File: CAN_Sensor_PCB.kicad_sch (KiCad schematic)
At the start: 63 parts, among them J1 Conn_01x02, J3 Conn_01x02, J4 Conn_01x04, J5 Conn_01x04, U1 APM32F405RGT6, U2 LM2594HVM-3.3, U5 LMV358

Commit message: VER1.0: добавил BOM и закупочный лист
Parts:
- C19: Product Name (none) -> 293D107X96R3B2TE3
- D4: Description P/N Yellow LED -> LED
- D5: value MBRA320 -> ~; Description P/N (none) -> Diode; Product Name (none) -> MBRA320
- D6: Description P/N Blue LED -> LED
- D7: Description P/N Blue LED -> LED; Product Name FYLS-0805UBC -> FYLS-0805PGC
- J1: value Conn_01x02 -> ~; Purpose (none) -> CAN; now not fitted
- J3: value Conn_01x02 -> ~; Purpose (none) -> PWR; now not fitted
- J4: value Conn_01x04 -> ~; Purpose (none) -> PT1; now not fitted
- J5: value Conn_01x04 -> ~; Purpose (none) -> PT2; now not fitted
- L1: Product Name (none) -> NLC453232T-470K-PF
- U1: value APM32F405RGT6 -> ~; Product Name (none) -> APM32F405RGT6
- U2: value LM2594HVM-3.3 -> ~; Product Name (none) -> LM2594HVM-3.3
- U5: value LMV358 -> ~; Product Name (none) -> LM158DR
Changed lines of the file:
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@@
 			)
 		)
-		(property "Value" "LMV358"
+		(property "Value" "~"
 			(at 149.86 267.462 0)
 			(effects
@@
 			)
 		)
+		(property "Product Name" "LM158DR"
+			(at 148.844 261.62 0)
+			(effects
+				(font
+					(size 1.27 1.27)
+				)
+			)
+		)
 		(pin "2"
 		)
@@
 		(in_bom yes)
 		(on_board yes)
-		(dnp no)
+		(dnp yes)
 		(property "Reference" "J5"
 			(at 107.95 255.27 0)
@@
 			)
 		)
-		(property "Value" "Conn_01x04"
+		(property "Value" "~"
 			(at 107.95 254 0)
 			(effects
@@
 			)
 		)
+		(property "Purpose" "PT2"
+			(at 107.95 267.97 0)
+			(effects
+				(font
+					(size 1.27 1.27)
+				)
+			)
+		)
 		(pin "4"
 		)
@@
 			)
 		)
-		(property "Description P/N" "Blue LED"
+		(property "Description P/N" "LED"
 			(at 139.7 156.21 0)
 			(effects
@@
 			)
 		)
+		(property "Product Name" "293D107X96R3B2TE3"
+			(at 334.01 142.875 0)
+			(effects
+				(font
+					(size 1.27 1.27)
+				)
+				(hide yes)
+			)
+		)
 		(pin "1"
 		)
@@
 		(on_board yes)
 		(dnp no)
-		(fields_autoplaced yes)
 		(property "Reference" "U5"
 			(at 90.17 234.95 90)
@@
 			)
 		)
-		(property "Value" "LMV358"
+		(property "Value" "~"
 			(at 90.17 237.49 90)
 			(effects
@@
 			)
 		)
+		(property "Product Name" "LM158DR"
+			(at 90.17 237.49 90)
+			(effects
+				(font
+					(size 1.27 1.27)
+				)
+			)
+		)
 		(pin "2"
 		)
@@
 			)
 		)
-		(property "Description P/N" "Yellow LED"
+		(property "Description P/N" "LED"
 			(at 355.6 140.97 0)
 			(effects
@@
 			)
 		)
-		(property "Value" "LMV358"
+		(property "Value" "~"
 			(at 64.77 266.7 0)
 			(effects
@@
 			)
 		)
+		(property "Product Name" "LM158DR"
+			(at 63.5 261.62 0)
+			(effects
+				(font
+					(size 1.27 1.27)
+				)
+			)
+		)
 		(pin "2"
 		)
@@
 			)
 		)
-		(property "Value" "APM32F405RGT6"
+		(property "Value" "~"
 			(at 118.11 165.608 0)
 			(effects
@@
 			)
 		)
+		(property "Product Name" "APM32F405RGT6"
+			(at 113.03 118.11 0)
+			(effects
+				(font
+					(size 1.27 1.27)
+				)
+			)
+		)
 		(pin "60"
 		)
@@
 			)
 		)
-		(property "Value" "MBRA320"
+		(property "Value" "~"
 			(at 327.66 143.891 90)
 			(effects
@@
 			)
 		)
+		(property "Product Name" "MBRA320"
+			(at 325.12 142.24 0)
+			(effects
+				(font
+					(size 1.27 1.27)
+				)
+				(hide yes)
+			)
+		)
+		(property "Description P/N" "Diode"
+			(at 325.12 142.24 0)
+			(effects
+				(font
+					(size 1.27 1.27)
+				)
+				(hide yes)
+			)
+		)
 		(pin "1"
 		)
@@
 			)
 		)
+		(property "Product Name" "NLC453232T-470K-PF"
+			(at 328.93 138.43 0)
+			(effects
+				(font
+					(size 1.27 1.27)
+				)
+				(hide yes)
+			)
+		)
 		(pin "1"
 		)
@@
 		(in_bom yes)
 		(on_board yes)
-		(dnp no)
+		(dnp yes)
 		(property "Reference" "J1"
 			(at 340.36 67.31 0)
@@
 			)
 		)
-		(property "Value" "Conn_01x02"
+		(property "Value" "~"
 			(at 342.9 62.23 0)
 			(effects
@@
 			)
 		)
+		(property "Purpose" "CAN"
+			(at 342.9 71.12 0)
+			(effects
+				(font
+					(size 1.27 1.27)
+				)
+			)
+		)
 		(pin "2"
 		)
@@
 		(in_bom yes)
 		(on_board yes)
-		(dnp no)
+		(dnp yes)
 		(property "Reference" "J3"
 			(at 269.24 142.24 0)
@@
 			)
 		)
-		(property "Value" "Conn_01x02"
+		(property "Value" "~"
 			(at 271.78 137.16 0)
 			(effects
@@
 			)
 		)
+		(property "Purpose" "PWR"
+			(at 271.78 146.05 0)
+			(effects
+				(font
+					(size 1.27 1.27)
+				)
+			)
+		)
 		(pin "2"
 		)
@@
 			)
 		)
-		(property "Description P/N" "Blue LED"
+		(property "Description P/N" "LED"
 			(at 146.05 156.21 0)
 			(effects
@@
 			)
 		)
-		(property "Product Name" "FYLS-0805UBC"
+		(property "Product Name" "FYLS-0805PGC"
 			(at 146.05 156.21 0)
 			(effects
@@
 		(on_board yes)
 		(dnp no)
-		(fields_autoplaced yes)
 		(property "Reference" "U2"
 			(at 311.15 128.27 0)
@@
 			)
 		)
-		(property "Value" "LM2594HVM-3.3"
+		(property "Value" "~"
 			(at 311.15 130.81 0)
 			(effects
@@
 			)
 		)
+		(property "Product Name" "LM2594HVM-3.3"
+			(at 311.15 131.826 0)
+			(effects
+				(font
+					(size 1.27 1.27)
+				)
+			)
+		)
 		(pin "1"
 		)
@@
 		(in_bom yes)
 		(on_board yes)
-		(dnp no)
+		(dnp yes)
 		(property "Reference" "J4"
 			(at 22.86 255.27 0)
@@
 			)
 		)
-		(property "Value" "Conn_01x04"
+		(property "Value" "~"
 			(at 22.86 254 0)
 			(effects
@@
 			)
 		)
+		(property "Purpose" "PT1"
+			(at 22.86 267.97 0)
+			(effects
+				(font
+					(size 1.27 1.27)
+				)
+			)
+		)

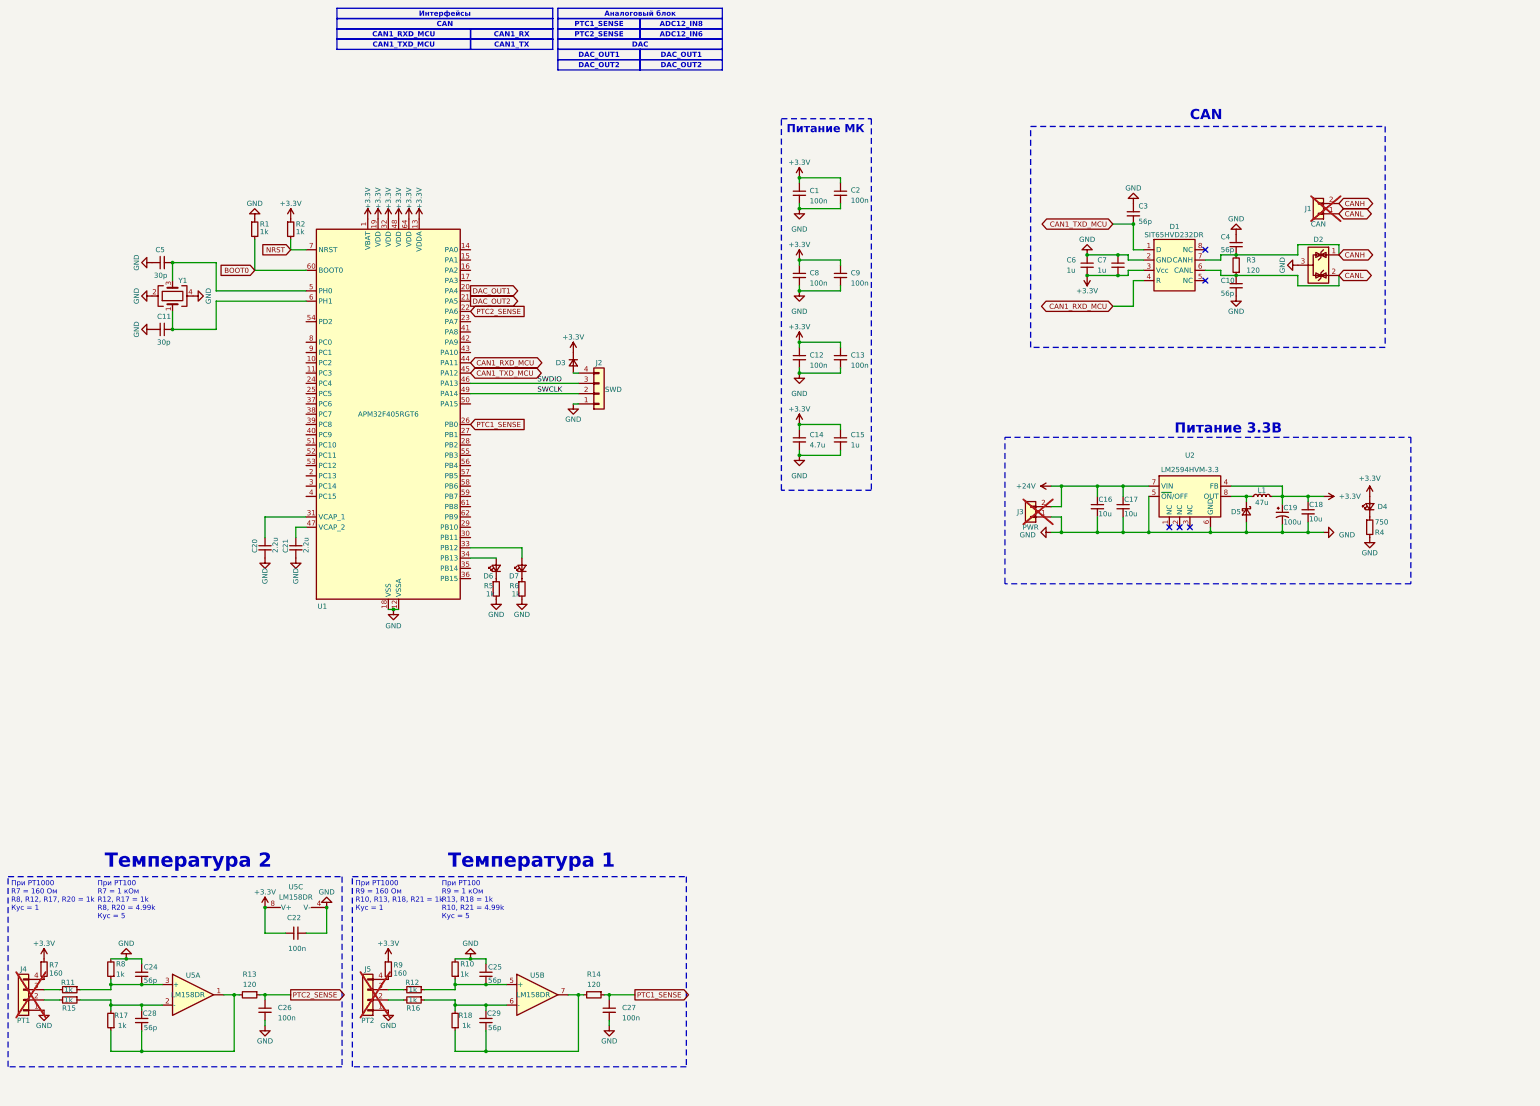
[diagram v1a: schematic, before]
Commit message: VER1.0: добавил схему по госту в доки
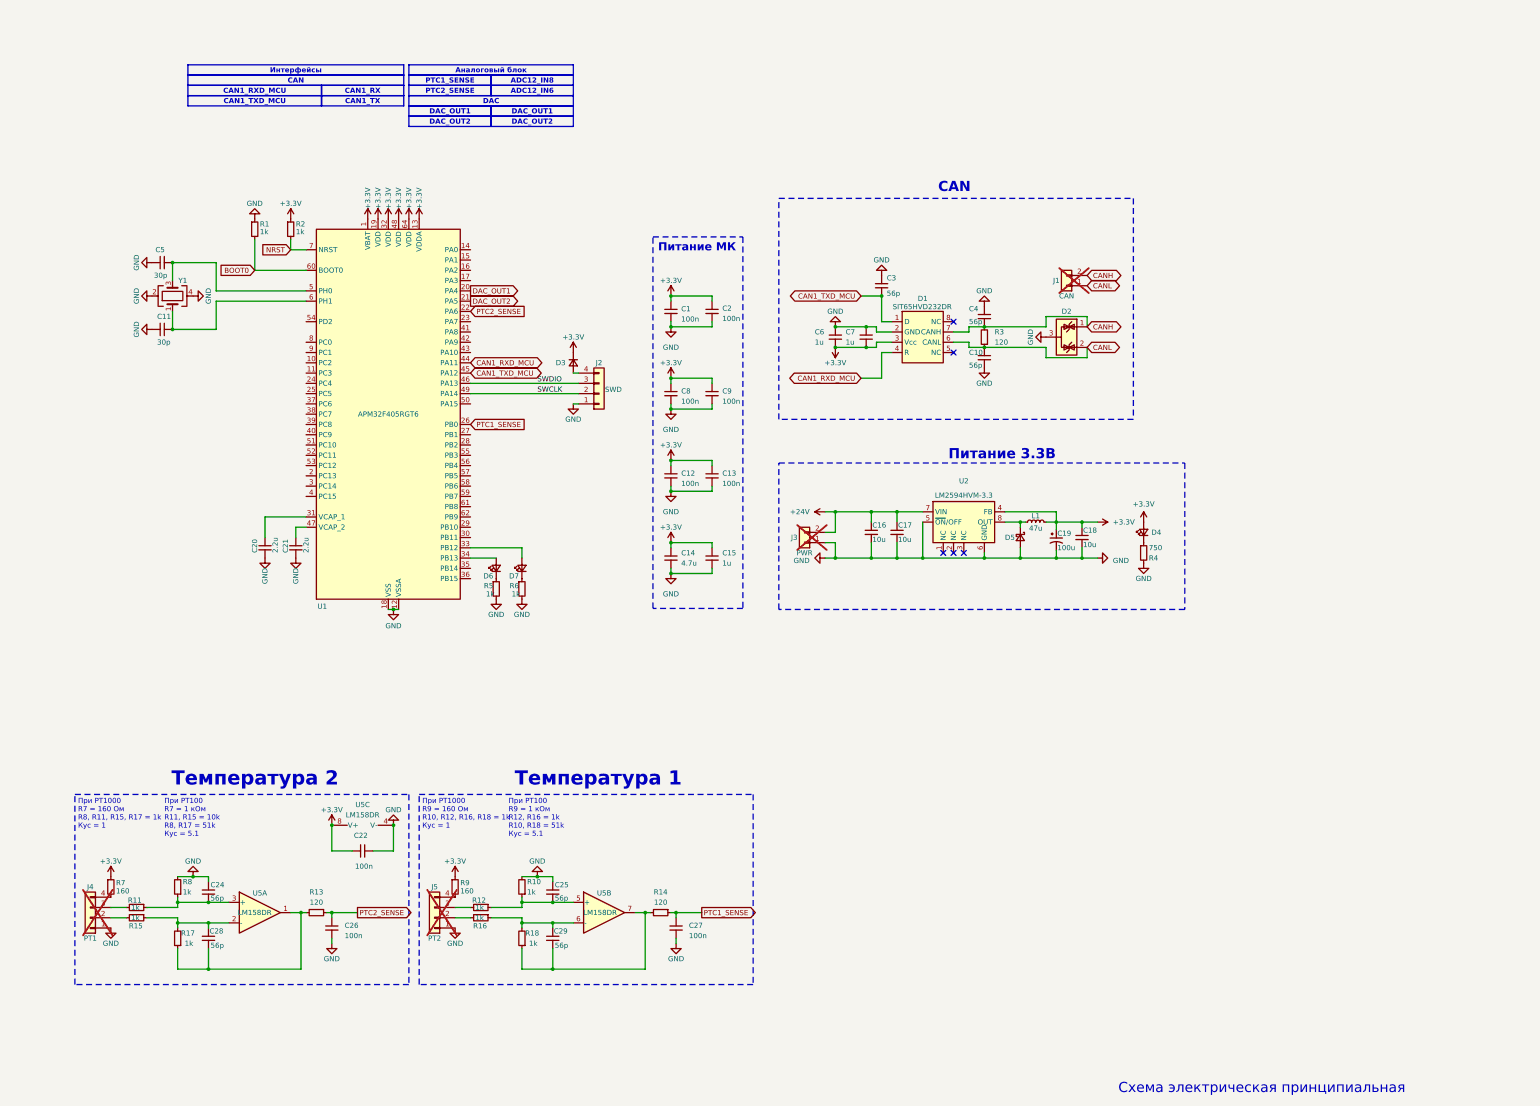
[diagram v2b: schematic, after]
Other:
- note added: "R10, R12, R16, R18 = 1k"
- note added: "R10, R18 = 51k"
- note added: "R11, R15 = 10k"
- note added: "R12, R16 = 1k"
- note added: "R8, R11, R15, R17 = 1k"
- note added: "R8, R17 = 51k"
- note added: "Кус = 5.1"
- note added: "Схема электрическая принципиальная"
- note removed: "R10, R13, R18, R21 = 1k"
- note removed: "R10, R21 = 4.99k"
- note removed: "R12, R17 = 1k"
- note removed: "R13, R18 = 1k"
- note removed: "R8, R12, R17, R20 = 1k"
- note removed: "R8, R20 = 4.99k"
- note removed: "Кус = 5"
- company: (none) -> ООО "Электротранспортные технологии"
- title: (none) -> Датчик температуры CAN
- moved on the sheet: C1, C10, C12, C13, C14, C15, C16, C17, C18, C19, C2, C22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

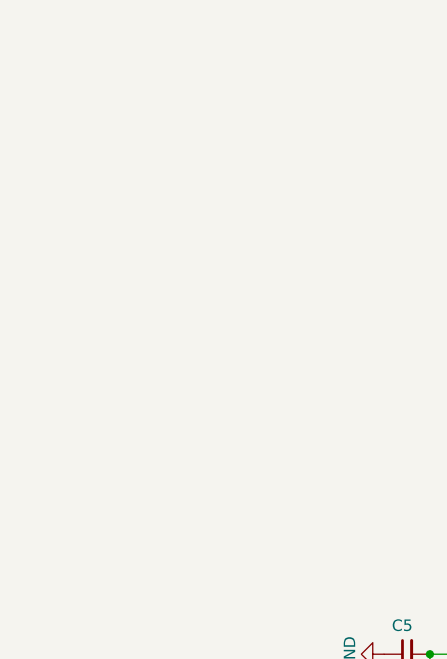
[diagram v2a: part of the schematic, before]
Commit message: VER1.0: исправил Э3
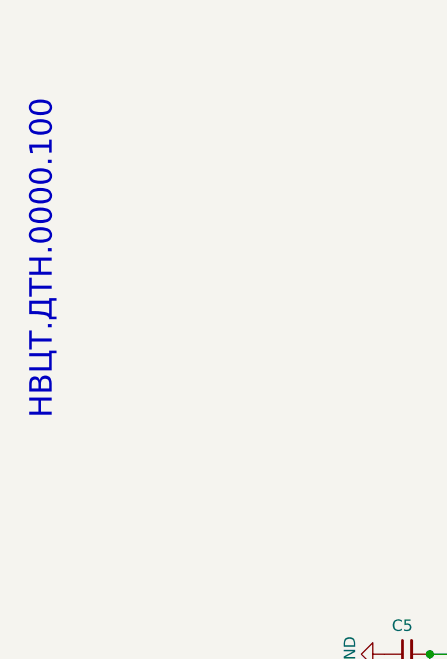
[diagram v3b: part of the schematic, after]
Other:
- note added: "НВЦТ.ДТН.0000.100"
- title: Датчик температуры CAN -> Плата датчика температуры CAN
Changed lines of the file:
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@@
 	(paper "A3")
 	(title_block
-		(title "Датчик температуры CAN")
+		(title "Плата датчика температуры CAN")
 		(company "ООО \"Электротранспортные технологии\"")
-		(comment 1 "НВЦТ.0001.0200.820 Э3")
+		(comment 1 "НВЦТ.ДТН.0000.100 Э3")
 		(comment 2 "Филатов А.С.")
 		(comment 3 "Сизякин А.В.")
@@
 		)
 	)
+	(text "НВЦТ.ДТН.0000.100"
+		(exclude_from_sim no)
+		(at 16.51 36.83 90)
+		(effects
+			(font
+				(size 2.5 2.5)
+			)
+		)
+	)

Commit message: VER21.0: исправил Э3
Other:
- note added: "1. Перечень элементов см. НВЦТ.ДТН.0000.100 ПЭ3."
- note added: "ООО "Электротранспортные"
- note added: "технологии""
- company: ООО "Электротранспортные технологии" -> (none)
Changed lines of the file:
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@@
 	(title_block
 		(title "Плата датчика температуры CAN")
-		(company "ООО \"Электротранспортные технологии\"")
 		(comment 1 "НВЦТ.ДТН.0000.100 Э3")
 		(comment 2 "Филатов А.С.")
@@
 	(text "Схема электрическая принципиальная"
 		(exclude_from_sim no)
-		(at 328.93 284.734 0)
+		(at 329.946 271.272 0)
 		(effects
 			(font
@@
 		)
 	)
+	(text "ООО \"Электротранспортные"
+		(exclude_from_sim no)
+		(at 389.89 282.702 0)
+		(effects
+			(font
+				(size 2.5 2.5)
+			)
+		)
+	)
 	(text "R9 = 160 Ом\n"
 		(exclude_from_sim no)
@@
 		)
 	)
+	(text "технологии\""
+		(exclude_from_sim no)
+		(at 389.89 287.02 0)
+		(effects
+			(font
+				(size 2.5 2.5)
+			)
+		)
+	)
 	(text "R11, R15 = 10k"
 		(exclude_from_sim no)
@@
 		)
 	)
+	(text "1. Перечень элементов см. НВЦТ.ДТН.0000.100 ПЭ3."
+		(exclude_from_sim no)
+		(at 282.702 213.106 0)
+		(effects
+			(font
+				(size 3.5 3.5)
+			)
+		)
+	)

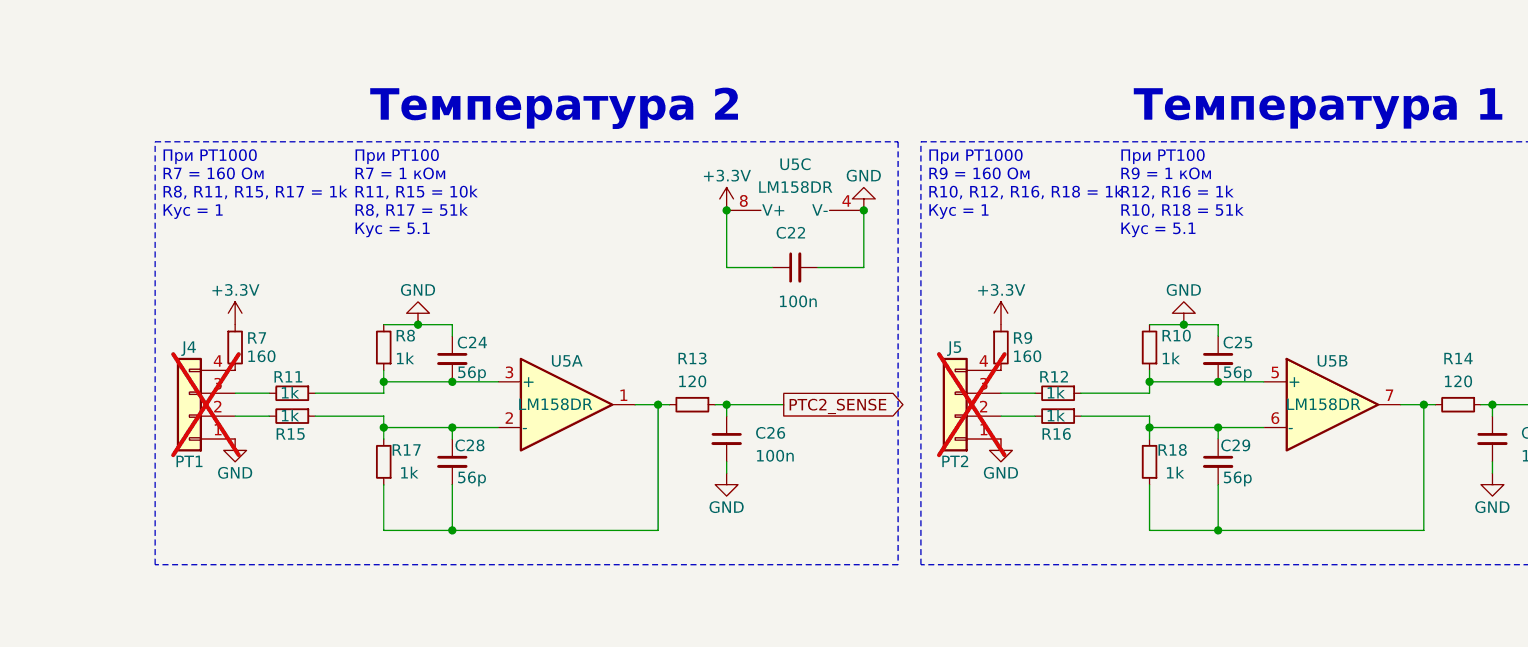
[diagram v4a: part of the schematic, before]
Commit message: VER1.0: исправил номиналы резисторов для датчика и BOM
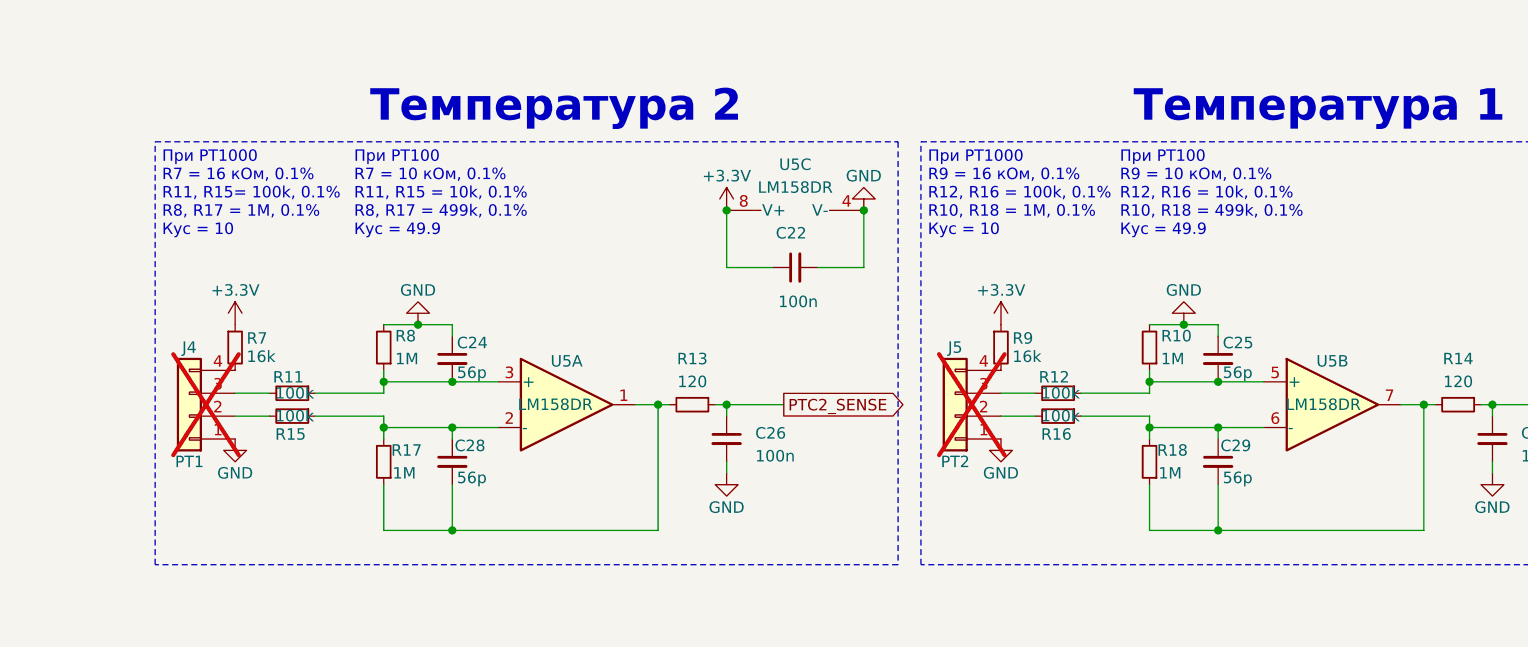
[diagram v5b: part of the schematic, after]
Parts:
- C1, C10, C11, C12, C13, C14, C15, C2, C20, C21, C22, C24, C25, C26, C27, C28, C29, C3, C4, C5, C6, C7, C8, C9: Description P/N (none) -> Capacitor SMD 10V+
- C16, C17, C18: Description P/N (none) -> Capacitor SMD 50V+
- C19: Description P/N (none) -> Tantalum Capacitor
- J1, J3, J4, J5: Description P/N (none) -> Connector
- L1: Description P/N (none) -> Inductor SMD
- R1, R13, R14, R2, R3, R4, R5, R6: Description P/N (none) -> Resistor SMD
- R10, R17, R18, R8: value 1k -> 1M; Description P/N (none) -> Resistor SMD 0.1%
- R11, R12, R15, R16: value 1k -> 100k; Description P/N (none) -> Resistor SMD 0.1%
- R7, R9: value 160 -> 16k; Description P/N (none) -> Resistor SMD 0.1%
- U1: Description P/N (none) -> uController
- U2: Description P/N (none) -> DCDC
- U5: Description P/N (none) -> OpAmp
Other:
- note added: "R10, R18 = 1M, 0.1%"
- note added: "R10, R18 = 499k, 0.1%"
- note added: "R11, R15 = 10k, 0.1%"
- note added: "R11, R15= 100k, 0.1%"
- note added: "R12, R16 = 100k, 0.1%"
- note added: "R12, R16 = 10k, 0.1%"
- note added: "R7 = 10 кОм, 0.1%"
- note added: "R7 = 16 кОм, 0.1%"
- note added: "R8, R17 = 1M, 0.1%"
- note added: "R8, R17 = 499k, 0.1%"
- note added: "R9 = 10 кОм, 0.1%"
- note added: "R9 = 16 кОм, 0.1%"
- note added: "Кус = 10"
- note added: "Кус = 49.9"
- note removed: "R10, R12, R16, R18 = 1k"
- note removed: "R10, R18 = 51k"
- note removed: "R11, R15 = 10k"
- note removed: "R12, R16 = 1k"
- note removed: "R7 = 1 кОм"
- note removed: "R7 = 160 Ом"
- note removed: "R8, R11, R15, R17 = 1k"
- note removed: "R8, R17 = 51k"
- note removed: "R9 = 1 кОм"
- note removed: "R9 = 160 Ом"
- note removed: "Кус = 1"
- note removed: "Кус = 5.1"
